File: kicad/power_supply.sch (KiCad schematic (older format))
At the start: 33 parts, among them P2 CONN_01X03, Q2 NDT2955, U2 MCP1700, U7 LM2672M-5.0, U8 LM358

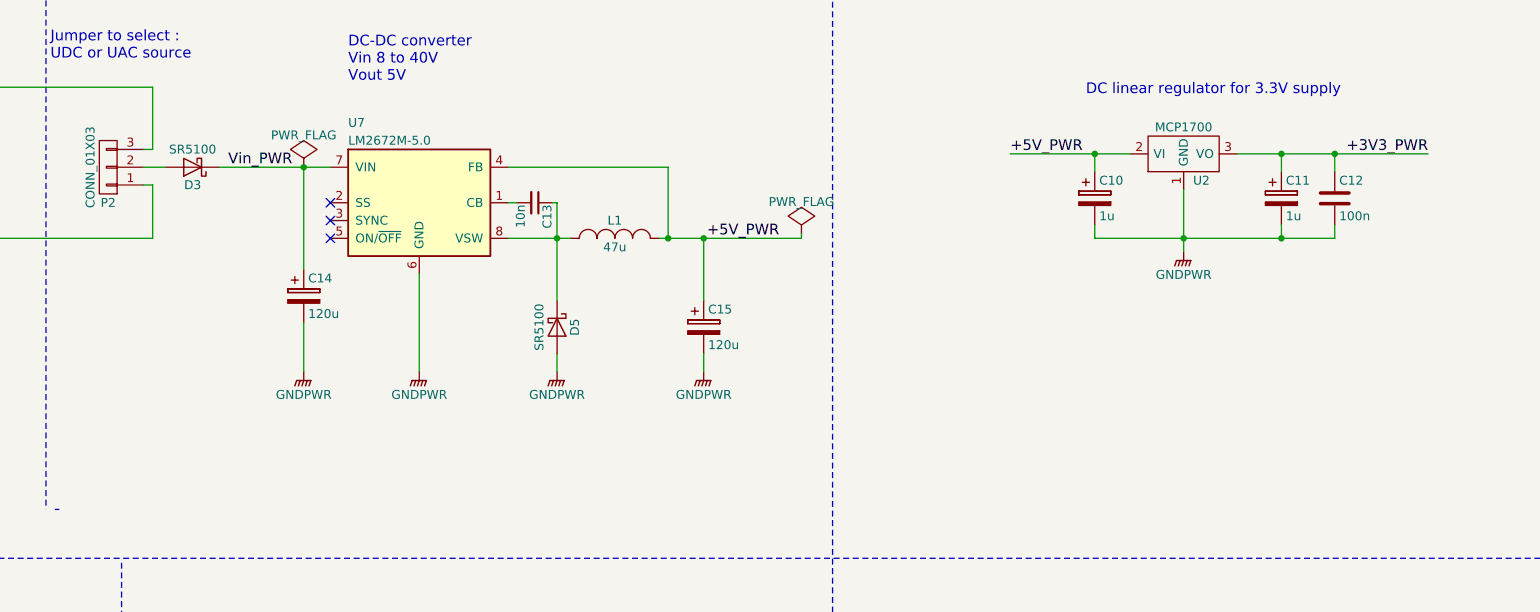
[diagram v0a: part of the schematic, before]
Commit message: add somes notes on schematics
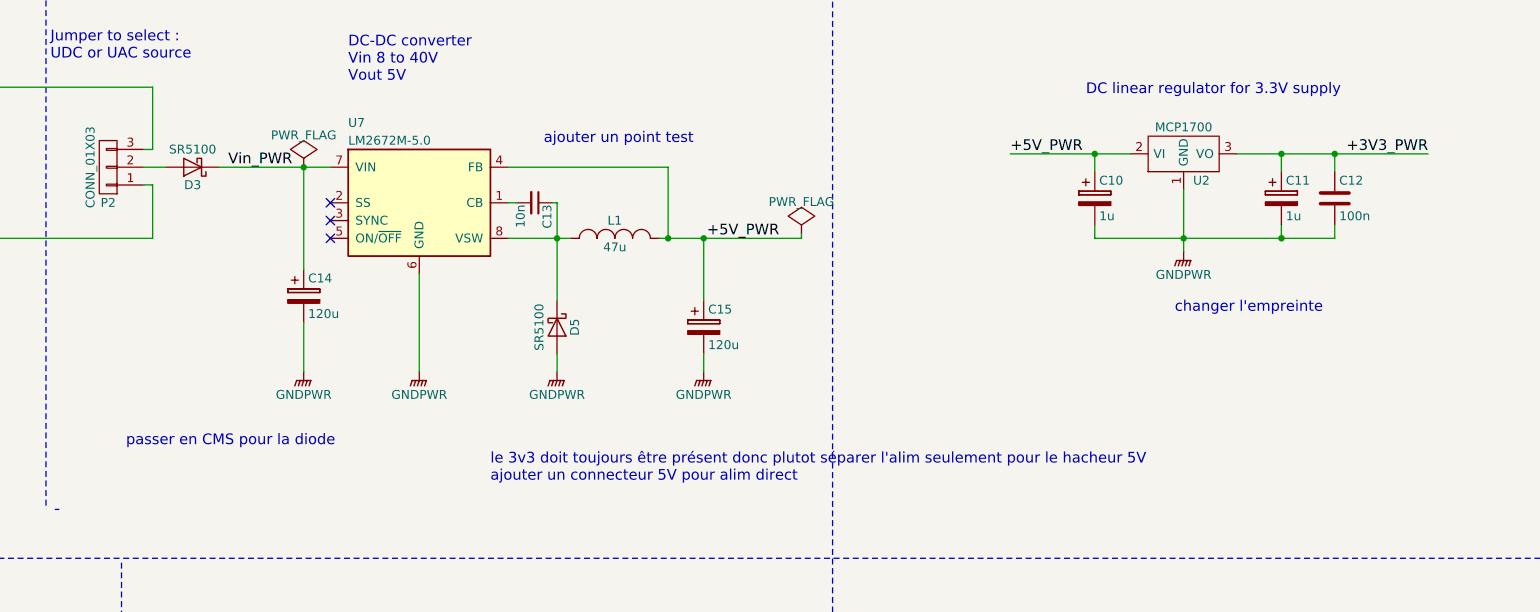
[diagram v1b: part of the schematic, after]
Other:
- note added: "ajouter un point test"
- note added: "changer l'empreinte"
- note added: "le 3v3 doit toujours être présent donc plutot séparer l'alim seulement pour le hacheur 5V\najouter un connecteur 5V pour alim direct"
- note added: "passer en CMS pour la diode"
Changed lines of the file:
@@
 Wire Wire Line
 	3525 2025 4150 2025
+Text Notes 3000 3600 0    60   ~ 0
+passer en CMS pour la diode
+Text Notes 5350 1900 0    60   ~ 0
+ajouter un point test
+Text Notes 5050 3800 0    60   ~ 0
+le 3v3 doit toujours être présent donc plutot séparer l'alim seulement pour le hacheur 5V\najouter un connecteur 5V pour alim direct
+Text Notes 8900 2850 0    60   ~ 0
+changer l'empreinte
 $EndSCHEMATC

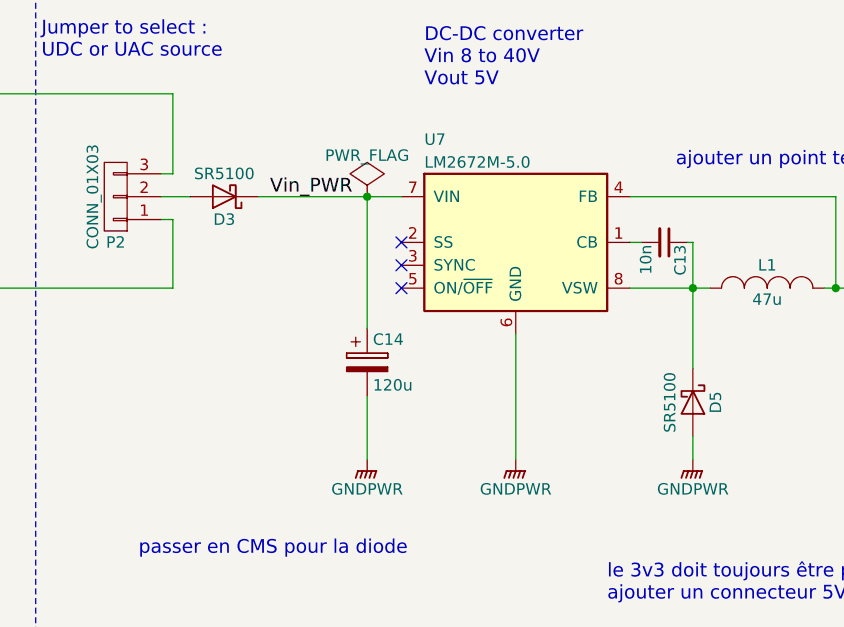
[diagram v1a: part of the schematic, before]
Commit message: change D3 and D5 for smd diode
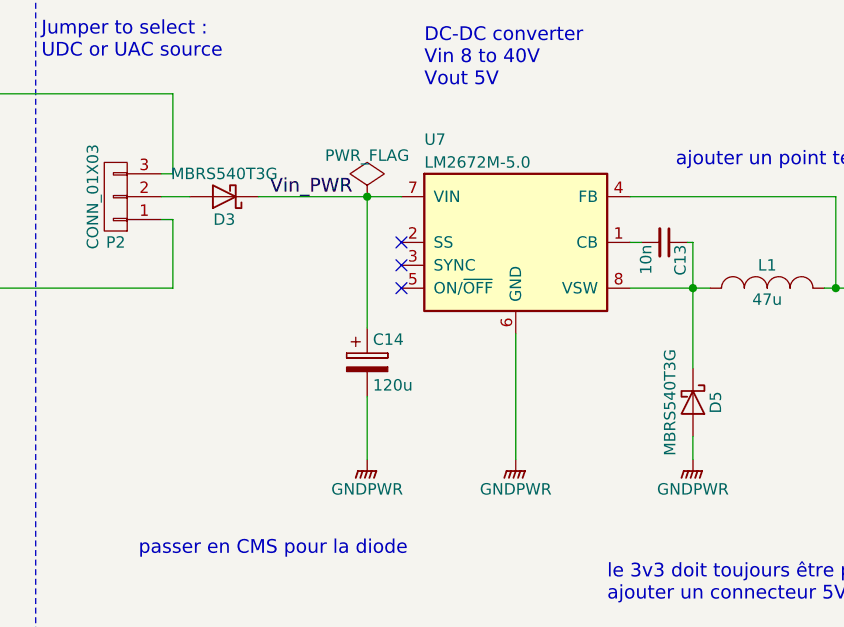
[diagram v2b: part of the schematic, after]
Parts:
- D3, D5: value SR5100 -> MBRS540T3G; footprint digital:Diode_DO-27_Horizontal_RM12 -> Diodes_SMD:SMC_Handsoldering
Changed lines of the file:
@@
 P 5425 2925
 F 0 "D5" H 5425 3025 50  0000 C CNN
-F 1 "SR5100" H 5425 2825 50  0000 C CNN
-F 2 "digital:Diode_DO-27_Horizontal_RM12" H 5425 2925 50  0001 C CNN
-F 3 "" H 5425 2925 50  0000 C CNN
+F 1 "MBRS540T3G" H 5425 2825 50  0000 C CNN
+F 2 "Diodes_SMD:SMC_Handsoldering" H 5425 2925 50  0001 C CNN
+F 3 "https://docs-emea.rs-online.com/webdocs/154f/0900766b8154f4f3.pdf" H 5425 2925 50  0001 C CNN
 	1    5425 2925
 	0    1    1    0
@@
 	1    2375 5400
 	1    0    0    -1
-$EndComp
-$Comp
-L D_Schottky D3
-U 1 1 58B82BAA
-P 3375 2025
-F 0 "D3" H 3375 2125 50  0000 C CNN
-F 1 "SR5100" H 3375 1925 50  0000 C CNN
-F 2 "digital:Diode_DO-27_Horizontal_RM12" H 3375 2025 50  0001 C CNN
-F 3 "" H 3375 2025 50  0000 C CNN
-	1    3375 2025
-	-1   0    0    1
 $EndComp
 NoConn ~ 4150 2225
@@
 Text Notes 8900 2850 0    60   ~ 0
 changer l'empreinte
+$Comp
+L D_Schottky D3
+U 1 1 5A806E74
+P 3375 2025
+F 0 "D3" H 3375 2125 50  0000 C CNN
+F 1 "MBRS540T3G" H 3375 1925 50  0000 C CNN
+F 2 "Diodes_SMD:SMC_Handsoldering" H 3375 2025 50  0001 C CNN
+F 3 "https://docs-emea.rs-online.com/webdocs/154f/0900766b8154f4f3.pdf" H 3375 2025 50  0001 C CNN
+	1    3375 2025
+	-1   0    0    1
+$EndComp
 $EndSCHEMATC

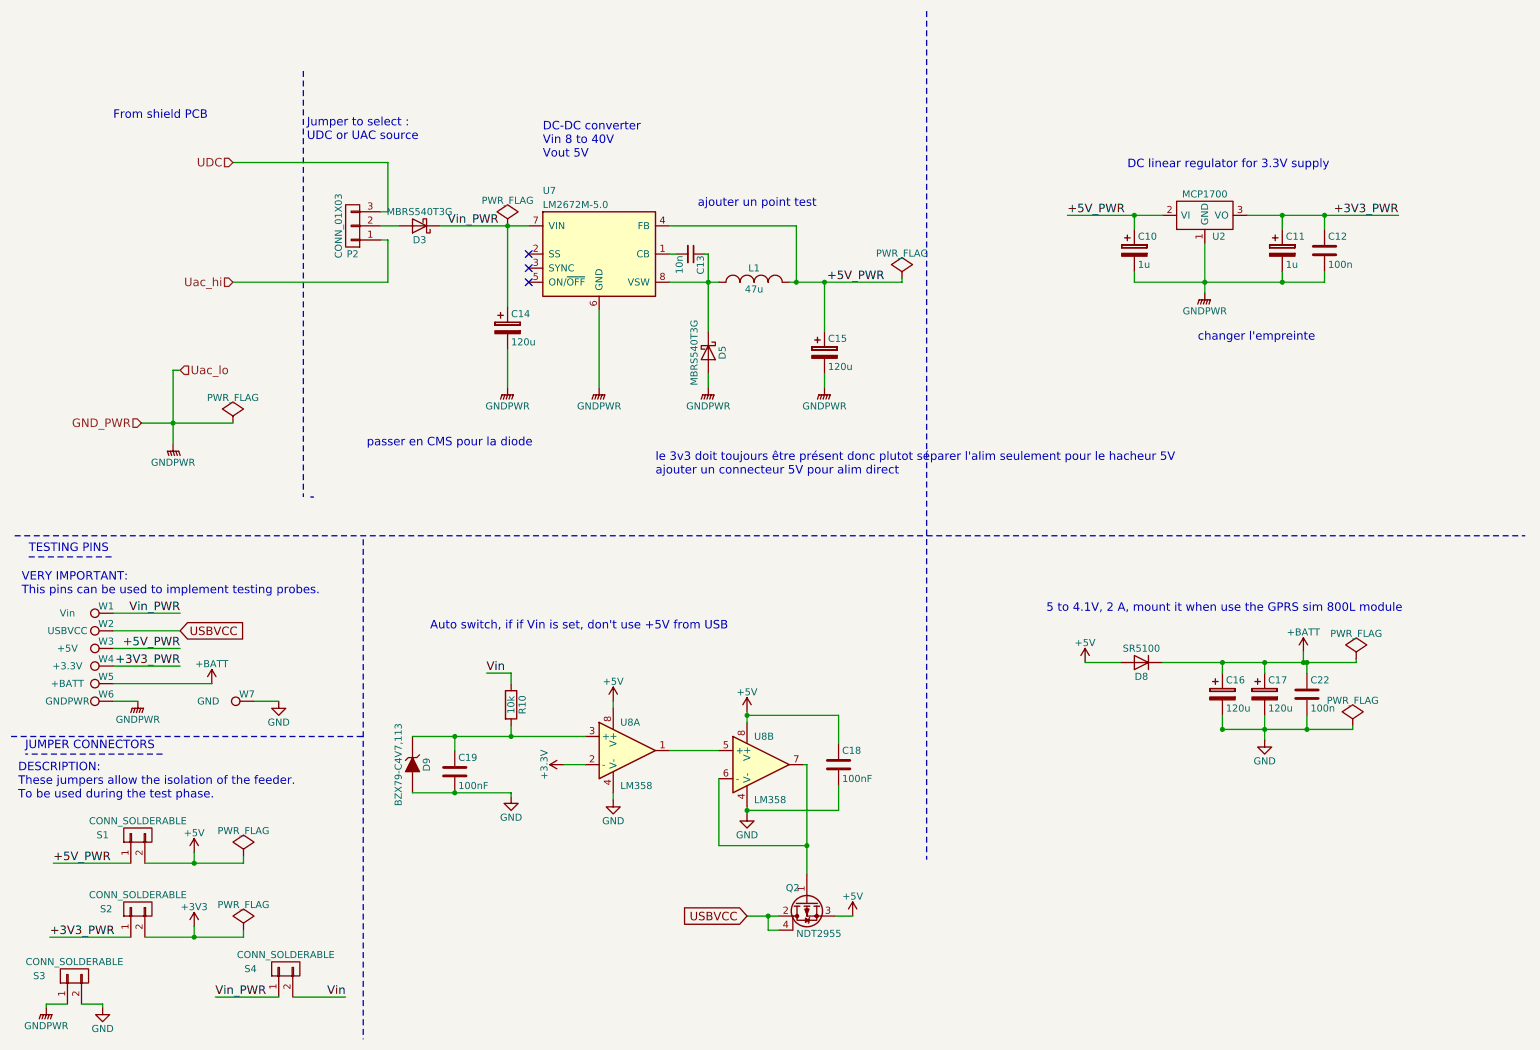
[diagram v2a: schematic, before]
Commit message: Modify micro pins and unify ground in power supply
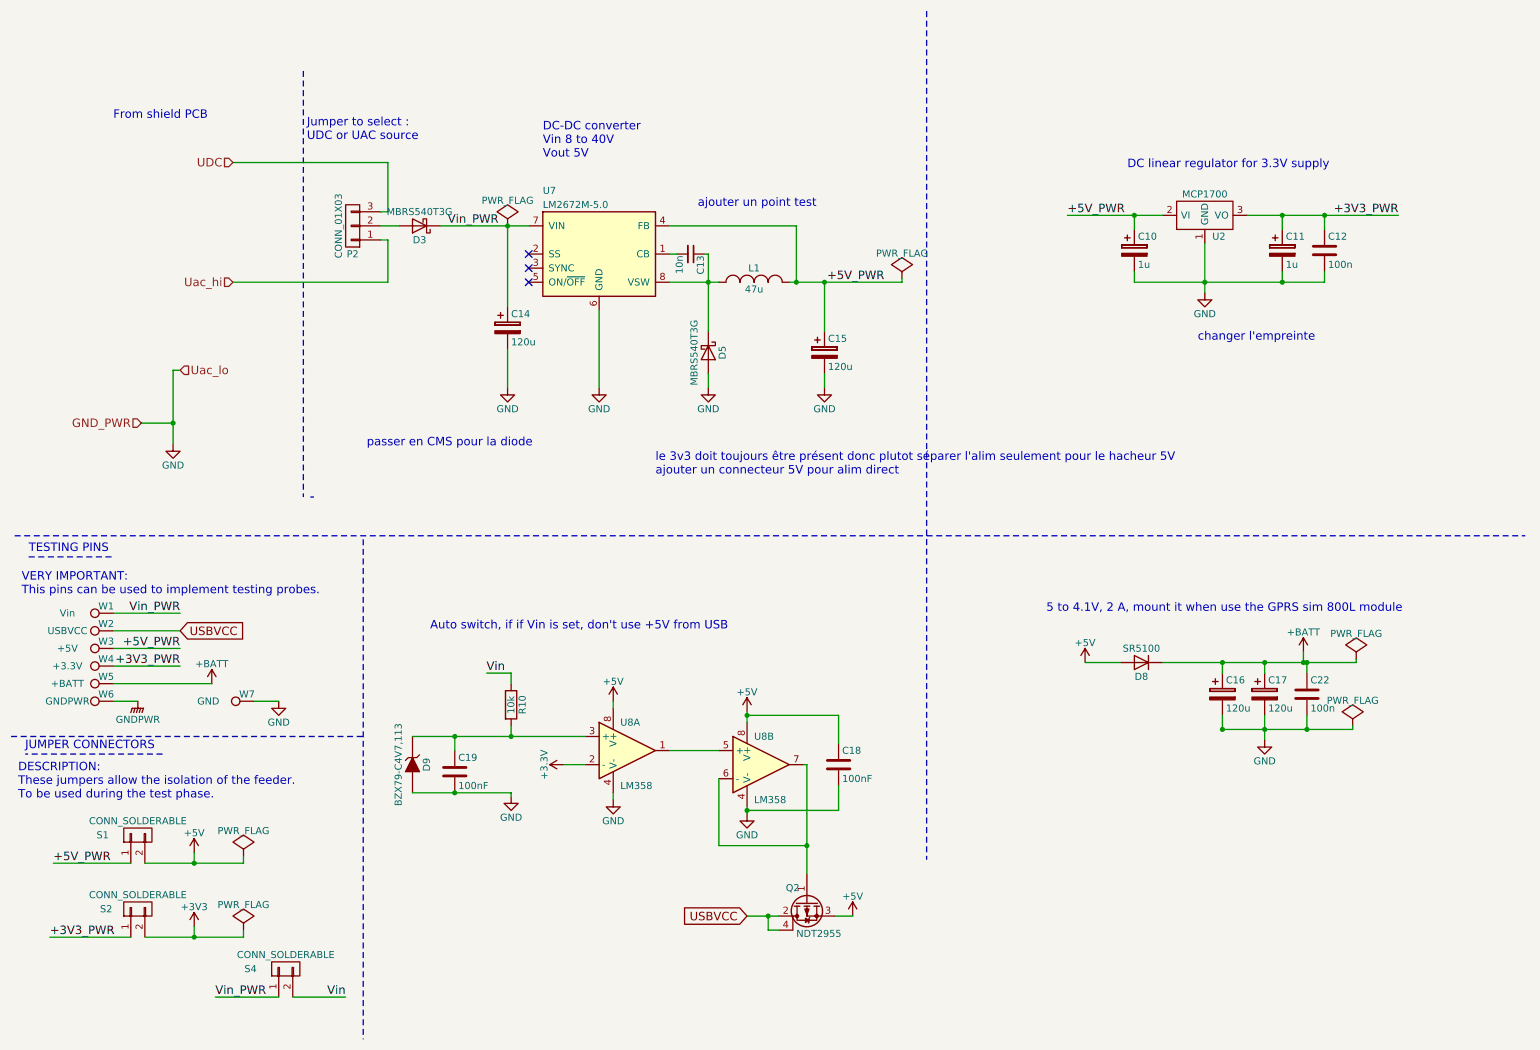
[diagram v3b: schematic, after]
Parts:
- removed S3: CONN_SOLDERABLE, digital:CONN_SOLDERABLE, symbol CONN_01X02
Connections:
- net GND: now also C10.2, C11.2, C12.2, C14.2, C15.2, D5.2 (A), U2.1 (GND), U7.6 (GND)
- net GNDPWR: no longer C10.2, C11.2, C12.2, C14.2, C15.2, D5.2 (A), U2.1 (GND), U7.6 (GND)
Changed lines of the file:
@@
 L GND #PWR039
 U 1 1 5886421D
-P 1125 7575
-F 0 "#PWR039" H 1125 7325 50  0001 C CNN
-F 1 "GND" H 1125 7425 50  0000 C CNN
-F 2 "" H 1125 7575 50  0000 C CNN
-F 3 "" H 1125 7575 50  0000 C CNN
-	1    1125 7575
+P 1625 3575
+F 0 "#PWR039" H 1625 3325 50  0001 C CNN
+F 1 "GND" H 1625 3425 50  0000 C CNN
+F 2 "" H 1625 3575 50  0000 C CNN
+F 3 "" H 1625 3575 50  0000 C CNN
+	1    1625 3575
 	1    0    0    -1
 $EndComp
@@
 $EndComp
 $Comp
-L GNDPWR #PWR047
-U 1 1 58B59C34
-P 8950 2500
-F 0 "#PWR047" H 8950 2300 50  0001 C CNN
-F 1 "GNDPWR" H 8950 2370 50  0000 C CNN
-F 2 "" H 8950 2450 50  0000 C CNN
-F 3 "" H 8950 2450 50  0000 C CNN
-	1    8950 2500
-	1    0    0    -1
-$EndComp
-$Comp
-L CONN_01X02 S3
-U 1 1 58B5A193
-P 925 7350
-F 0 "S3" V 925 7600 50  0000 C CNN
-F 1 "CONN_SOLDERABLE" V 1025 7350 50  0000 C CNN
-F 2 "digital:CONN_SOLDERABLE" H 925 7350 50  0001 C CNN
-F 3 "" H 925 7350 50  0000 C CNN
-	1    925  7350
-	0    -1   -1   0
-$EndComp
-$Comp
 L PWR_FLAG #FLG048
 U 1 1 58B5D8E8
@@
 F 3 "" H 4000 2750 50  0000 C CNN
 	1    4000 2750
-	1    0    0    -1
-$EndComp
-$Comp
-L GNDPWR #PWR049
-U 1 1 58B74994
-P 4000 3175
-F 0 "#PWR049" H 4000 2975 50  0001 C CNN
-F 1 "GNDPWR" H 4000 3045 50  0000 C CNN
-F 2 "" H 4000 3125 50  0000 C CNN
-F 3 "" H 4000 3125 50  0000 C CNN
-	1    4000 3175
-	1    0    0    -1
-$EndComp
-$Comp
-L GNDPWR #PWR050
-U 1 1 58B74E00
-P 4650 3175
-F 0 "#PWR050" H 4650 2975 50  0001 C CNN
-F 1 "GNDPWR" H 4650 3045 50  0000 C CNN
-F 2 "" H 4650 3125 50  0000 C CNN
-F 3 "" H 4650 3125 50  0000 C CNN
-	1    4650 3175
 	1    0    0    -1
 $EndComp
@@
 $EndComp
 $Comp
-L GNDPWR #PWR051
-U 1 1 58B750BB
-P 5425 3175
-F 0 "#PWR051" H 5425 2975 50  0001 C CNN
-F 1 "GNDPWR" H 5425 3045 50  0000 C CNN
-F 2 "" H 5425 3125 50  0000 C CNN
-F 3 "" H 5425 3125 50  0000 C CNN
-	1    5425 3175
-	1    0    0    -1
-$EndComp
-$Comp
 L INDUCTOR_SMALL L1
 U 1 1 58B753FD
@@
 F 3 "" H 6250 2925 50  0000 C CNN
 	1    6250 2925
-	1    0    0    -1
-$EndComp
-$Comp
-L GNDPWR #PWR052
-U 1 1 58B75B3D
-P 6250 3175
-F 0 "#PWR052" H 6250 2975 50  0001 C CNN
-F 1 "GNDPWR" H 6250 3045 50  0000 C CNN
-F 2 "" H 6250 3125 50  0000 C CNN
-F 3 "" H 6250 3125 50  0000 C CNN
-	1    6250 3175
 	1    0    0    -1
 $EndComp
@@
 	1775 7075 1775 7000
 Wire Wire Line
-	975  7550 1125 7550
-Wire Wire Line
-	1125 7550 1125 7575
-Wire Wire Line
 	2125 7075 2125 7025
 Connection ~ 1775 7075
@@
 Wire Wire Line
 	3150 2125 3150 2425
-Wire Wire Line
-	1400 3425 2050 3425
-Connection ~ 1625 3425
 Text Notes 1200 1275 0    60   ~ 0
 From shield PCB
@@
 $EndComp
 $Comp
-L GNDPWR #PWR065
-U 1 1 58B8E122
-P 725 7575
-F 0 "#PWR065" H 725 7375 50  0001 C CNN
-F 1 "GNDPWR" H 725 7445 50  0000 C CNN
-F 2 "" H 725 7525 50  0000 C CNN
-F 3 "" H 725 7525 50  0000 C CNN
-	1    725  7575
-	1    0    0    -1
-$EndComp
-Wire Wire Line
-	725  7575 725  7550
-Wire Wire Line
-	725  7550 875  7550
-$Comp
-L PWR_FLAG #FLG066
-U 1 1 58B9A4C8
-P 2050 3425
-F 0 "#FLG066" H 2050 3520 50  0001 C CNN
-F 1 "PWR_FLAG" H 2050 3605 50  0000 C CNN
-F 2 "" H 2050 3425 50  0000 C CNN
-F 3 "" H 2050 3425 50  0000 C CNN
-	1    2050 3425
-	1    0    0    -1
-$EndComp
-$Comp
 L PWR_FLAG #FLG067
 U 1 1 58B9B6B2
@@
 Text Label 1675 4775 2    60   ~ 0
 Vin_PWR
-$Comp
-L GNDPWR #PWR057
-U 1 1 58B59717
-P 1625 3575
-F 0 "#PWR057" H 1625 3375 50  0001 C CNN
-F 1 "GNDPWR" H 1625 3445 50  0000 C CNN
-F 2 "" H 1625 3525 50  0000 C CNN
-F 3 "" H 1625 3525 50  0000 C CNN
-	1    1625 3575
-	-1   0    0    -1
-$EndComp
 Wire Wire Line
 	1675 3050 1625 3050
@@
 	-1   0    0    1
 $EndComp
+Wire Wire Line
+	1400 3425 1625 3425
+Connection ~ 1625 3425
+$Comp
+L GND #PWR?
+U 1 1 5A858913
+P 4000 3175
+F 0 "#PWR?" H 4000 2925 50  0001 C CNN
+F 1 "GND" H 4000 3025 50  0000 C CNN
+F 2 "" H 4000 3175 50  0000 C CNN
+F 3 "" H 4000 3175 50  0000 C CNN
+	1    4000 3175
+	1    0    0    -1
+$EndComp
+$Comp
+L GND #PWR?
+U 1 1 5A8589E4
+P 4650 3175
+F 0 "#PWR?" H 4650 2925 50  0001 C CNN
+F 1 "GND" H 4650 3025 50  0000 C CNN
+F 2 "" H 4650 3175 50  0000 C CNN
+F 3 "" H 4650 3175 50  0000 C CNN
+	1    4650 3175
+	1    0    0    -1
+$EndComp
+$Comp
+L GND #PWR?
+U 1 1 5A858AD6
+P 5425 3175
+F 0 "#PWR?" H 5425 2925 50  0001 C CNN
+F 1 "GND" H 5425 3025 50  0000 C CNN
+F 2 "" H 5425 3175 50  0000 C CNN
+F 3 "" H 5425 3175 50  0000 C CNN
+	1    5425 3175
+	1    0    0    -1
+$EndComp
+$Comp
+L GND #PWR?
+U 1 1 5A858B86
+P 6250 3175
+F 0 "#PWR?" H 6250 2925 50  0001 C CNN
+F 1 "GND" H 6250 3025 50  0000 C CNN
+F 2 "" H 6250 3175 50  0000 C CNN
+F 3 "" H 6250 3175 50  0000 C CNN
+	1    6250 3175
+	1    0    0    -1
+$EndComp
+$Comp
+L GND #PWR?
+U 1 1 5A858BF4
+P 8950 2500
+F 0 "#PWR?" H 8950 2250 50  0001 C CNN
+F 1 "GND" H 8950 2350 50  0000 C CNN
+F 2 "" H 8950 2500 50  0000 C CNN
+F 3 "" H 8950 2500 50  0000 C CNN
+	1    8950 2500
+	1    0    0    -1
+$EndComp
 $EndSCHEMATC
